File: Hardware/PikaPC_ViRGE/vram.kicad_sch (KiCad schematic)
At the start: 70 parts, among them U2 86C325, U4 T224162B, U5 T224162B, U6 T224162B, U7 T224162B

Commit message: ViRGE card start PCB layout
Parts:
- R38, R39, R40, R41, R42, R43, R44, R45, R46, R47, R48, R49, R50, R51, R52, R53, R54, R55, R56, R57, R58, R59, R60, R61, R62, R63, R64, R65: footprint PikaPC_ViRGE:Resistor Option 0805 -> Resistor_SMD:R_0805_2012Metric
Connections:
- net VMD0: now also U4.31 (D8); no longer U4.2 (D0)
- net VMD1: now also U4.32 (D9); no longer U4.3 (D1)
- net VMD10: now also U4.4 (D2); no longer U4.33 (D10)
- net VMD11: now also U4.5 (D3); no longer U4.34 (D11)
- net VMD12: now also U4.7 (D4); no longer U4.36 (D12)
- net VMD13: now also U4.8 (D5); no longer U4.37 (D13)
- net VMD14: now also U4.9 (D6); no longer U4.38 (D14)
- net VMD15: now also U4.10 (D7); no longer U4.39 (D15)
- net VMD16: now also U6.31 (D8); no longer U6.2 (D0)
- net VMD17: now also U6.32 (D9); no longer U6.3 (D1)
- net VMD18: now also U6.33 (D10); no longer U6.4 (D2)
- net VMD19: now also U6.34 (D11); no longer U6.5 (D3)
- net VMD2: now also U4.33 (D10); no longer U4.4 (D2)
- net VMD20: now also U6.36 (D12); no longer U6.7 (D4)
- net VMD21: now also U6.37 (D13); no longer U6.8 (D5)
- net VMD22: now also U6.38 (D14); no longer U6.9 (D6)
- net VMD23: now also U6.39 (D15); no longer U6.10 (D7)
- net VMD24: now also U6.2 (D0); no longer U6.31 (D8)
- net VMD25: now also U6.3 (D1); no longer U6.32 (D9)
- net VMD26: now also U6.4 (D2); no longer U6.33 (D10)
- net VMD27: now also U6.5 (D3); no longer U6.34 (D11)
- net VMD28: now also U6.7 (D4); no longer U6.36 (D12)
- net VMD29: now also U6.8 (D5); no longer U6.37 (D13)
- net VMD3: now also U4.34 (D11); no longer U4.5 (D3)
- net VMD30: now also U6.9 (D6); no longer U6.38 (D14)
- net VMD31: now also U6.10 (D7); no longer U6.39 (D15)
- net VMD4: now also U4.36 (D12); no longer U4.7 (D4)
- net VMD5: now also U4.37 (D13); no longer U4.8 (D5)
- net VMD6: now also U4.38 (D14); no longer U4.9 (D6)
- net VMD7: now also U4.39 (D15); no longer U4.10 (D7)
- net VMD8: now also U4.2 (D0); no longer U4.31 (D8)
- net VMD9: now also U4.3 (D1); no longer U4.32 (D9)
- net ~{VMCAS0R}: now also U4.28 (~{CASH})
- net ~{VMCAS0}: no longer U4.29 (~{CASL})
- net ~{VMCAS1R}: now also U4.29 (~{CASL})
- net ~{VMCAS1}: no longer U4.28 (~{CASH})
- net ~{VMCAS2R}: now also U6.28 (~{CASH})
- net ~{VMCAS2}: no longer U6.29 (~{CASL})
- net ~{VMCAS3R}: now also U6.29 (~{CASL})
- net ~{VMCAS3}: no longer U6.28 (~{CASH})
- net ~{VMCAS4R}: now also U5.29 (~{CASL})
- net ~{VMCAS4}: no longer U5.29 (~{CASL})
- net ~{VMCAS5R}: now also U5.28 (~{CASH})
- net ~{VMCAS5}: no longer U5.28 (~{CASH})
- net ~{VMCAS6R}: now also U7.29 (~{CASL})
- net ~{VMCAS6}: no longer U7.29 (~{CASL})
- net ~{VMCAS7R}: now also U7.28 (~{CASH})
- net ~{VMCAS7}: no longer U7.28 (~{CASH})

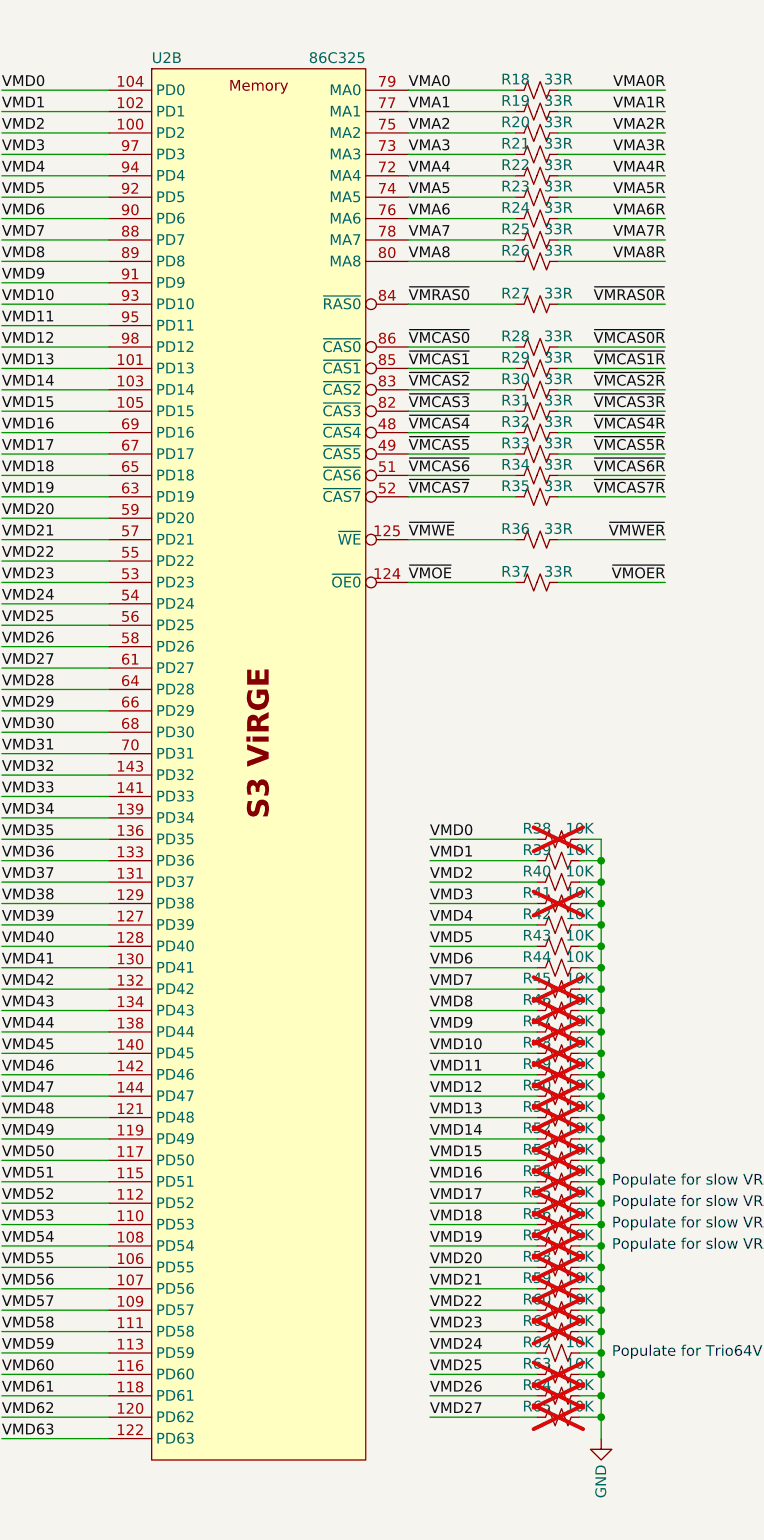
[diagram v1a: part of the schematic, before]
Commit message: ViRGE card PCB layout
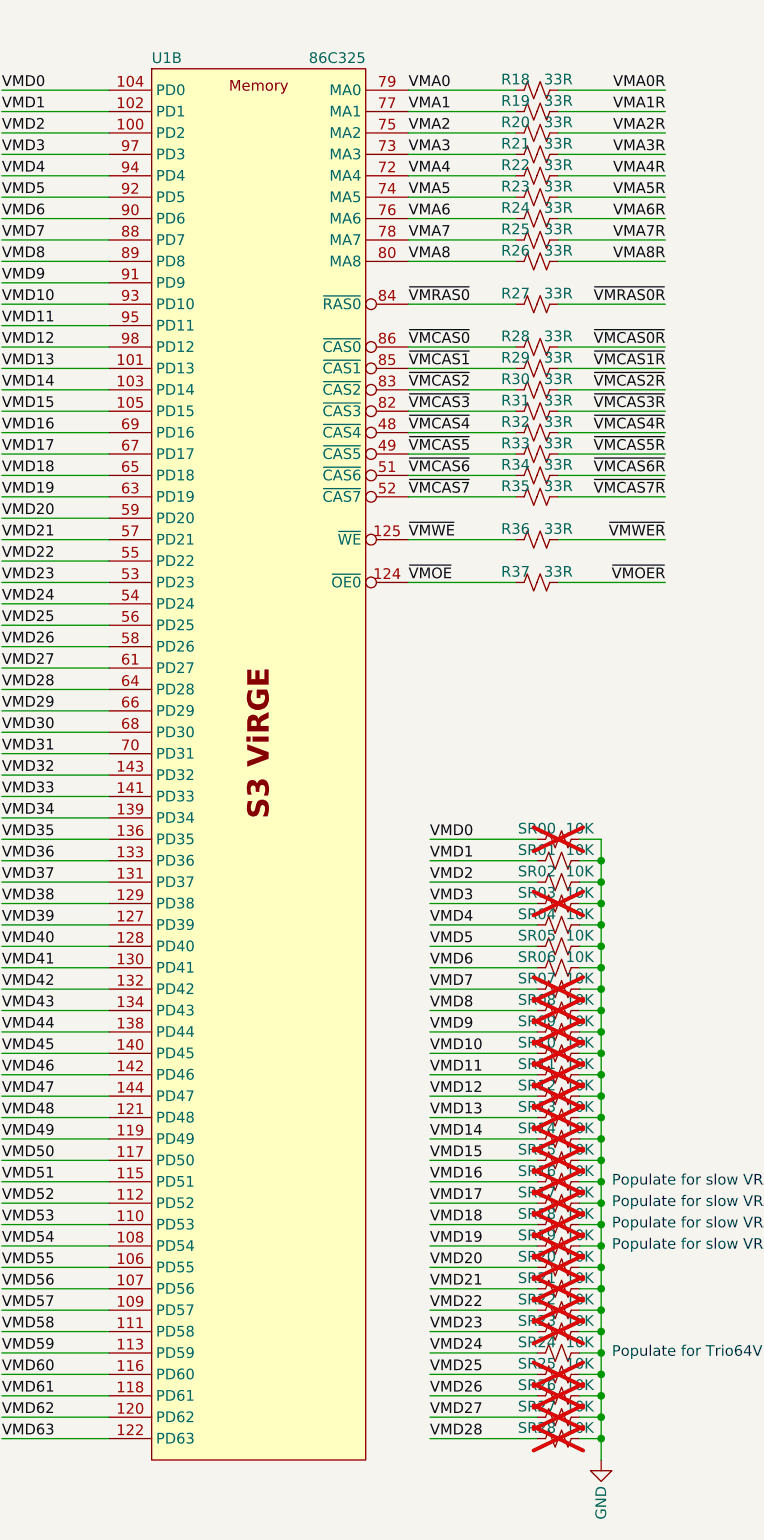
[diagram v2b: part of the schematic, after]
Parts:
- added SR28: 10K, Resistor_SMD:R_0805_2012Metric, symbol Device:R_Small_US
- renumbered R38 to SR00, R39 to SR01, R40 to SR02, R41 to SR03, R42 to SR04, R43 to SR05, R44 to SR06, R45 to SR07, R46 to SR08, R47 to SR09, R48 to SR10, R49 to SR11, R50 to SR12, R51 to SR13, R52 to SR14, R53 to SR15, R54 to SR16, R55 to SR17, R56 to SR18, R57 to SR19, R58 to SR20, R59 to SR21, R60 to SR22, R61 to SR23, R62 to SR24, R63 to SR25, R64 to SR26, R65 to SR27, U2 to U1
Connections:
- net GND: now also SR28.2
- net VMD28: now also SR28.1

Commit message: Prep for output
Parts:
- C23, C24, C32, C33: Mouser (none) -> 187-CL21B105KOFNNNG
- C25, C26, C27, C28, C29, C30, C34, C35, C36, C37, C38, C39: Mouser (none) -> 187-CL21B104KACNNNC
- R18, R19, R20, R21, R22, R23, R24, R25, R26, R27, R28, R29, R30, R31, R32, R33, R34, R35, R36, R37: Mouser (none) -> 603-RC0805JR-1033RL
- SR00, SR01, SR02, SR03, SR04, SR05, SR06, SR07, SR08, SR09, SR10, SR11, SR12, SR13, SR14, SR15, SR16, SR17, SR18, SR19, SR20, SR21, SR22, SR23, SR24, SR25, SR26, SR27, SR28: Mouser (none) -> 303-0805S8J0103T5E
